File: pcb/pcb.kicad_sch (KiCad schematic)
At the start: 235 parts, among them J1 Conn_01x30

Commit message: Daughterboard
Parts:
- added H52, H53, H54, H55, H56, H57, H58: MountingHole, symbol Mechanical:MountingHole
- added MX059.2, MX079.2, MX099.2: MX-NoLED, MX_Only:MXOnly-1U-NoLED, symbol MX_Alps_Hybrid:MX-NoLED
- renumbered SCRL1 to CAP1, CAP1 to NUM1, NUM1 to SCRL1
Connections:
- net CAPS_LED: now also CAP1.2 (A), J1.29 (Pin_29); no longer J1.5 (Pin_5), NUM1.2 (A)
- net COL0: now also J1.28 (Pin_28); no longer J1.8 (Pin_8)
- net COL1: now also J1.27 (Pin_27); no longer J1.9 (Pin_9)
- net COL2: now also J1.26 (Pin_26); no longer J1.10 (Pin_10)
- net COL3: now also J1.23 (Pin_23); no longer J1.11 (Pin_11)
- net COL4: now also J1.22 (Pin_22); no longer J1.12 (Pin_12)
- net COL5: now also J1.11 (Pin_11); no longer J1.13 (Pin_13)
- net COL6: now also J1.10 (Pin_10); no longer J1.14 (Pin_14)
- net COL7: now also J1.7 (Pin_7); no longer J1.15 (Pin_15)
- net COL8: now also J1.5 (Pin_5); no longer J1.16 (Pin_16)
- net COL9: now also J1.4 (Pin_4), MX059.2.1 (COL), MX079.2.1 (COL), MX099.2.1 (COL); no longer J1.17 (Pin_17)
- net NUM_LED: now also J1.3 (Pin_3), NUM1.2 (A); no longer J1.7 (Pin_7), SCRL1.2 (A)
- net RE1: now also J1.9 (Pin_9); no longer J1.2 (Pin_2)
- net RE2: now also J1.8 (Pin_8); no longer J1.3 (Pin_3)
- net RE3: now also J1.6 (Pin_6); no longer J1.4 (Pin_4)
- net ROW0: now also J1.25 (Pin_25); no longer J1.18 (Pin_18)
- net ROW1: now also J1.21 (Pin_21); no longer J1.19 (Pin_19)
- net ROW10: now also J1.13 (Pin_13); no longer J1.28 (Pin_28)
- net ROW11: now also J1.12 (Pin_12); no longer J1.29 (Pin_29)
- net ROW3: now also J1.19 (Pin_19); no longer J1.21 (Pin_21)
- net ROW4: now also J1.18 (Pin_18); no longer J1.22 (Pin_22)
- net ROW5: now also J1.17 (Pin_17); no longer J1.23 (Pin_23)
- net ROW7: now also J1.16 (Pin_16); no longer J1.25 (Pin_25)
- net ROW8: now also J1.15 (Pin_15); no longer J1.26 (Pin_26)
- net ROW9: now also J1.14 (Pin_14); no longer J1.27 (Pin_27)
- net SCRL_LED: now also J1.2 (Pin_2), SCRL1.2 (A); no longer CAP1.2 (A), J1.6 (Pin_6)
- net at D36.1 (A), MX026.2 (ROW): no longer MX086.1.2 (ROW)
- net at D53.2 (A), MX099.2 (ROW): now also MX099.2.2 (ROW)
- net at D41.1 (A), MX086.2 (ROW): now also MX086.1.2 (ROW)
- net at D49.2 (A), MX059.2 (ROW): now also MX059.2.2 (ROW)
- net at D42.1 (A), MX096.2 (ROW): now also MX096.275.2 (ROW)
- net at D51.2 (A), MX079.2 (ROW): now also MX079.2.2 (ROW)
- net at D37.1 (A), MX036.2 (ROW), MX036.2.2 (ROW): no longer MX096.275.2 (ROW)
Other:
- moved on the sheet: MX086.1, MX096.275

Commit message: daughterboard rewire
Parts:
- renumbered MX052 to MX112, MX053 to MX113, MX053.7 to MX113.7, MX054 to MX114, MX055 to MX115
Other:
- moved on the sheet: D17, D28, MX112, MX113, MX113.7, MX114, MX115

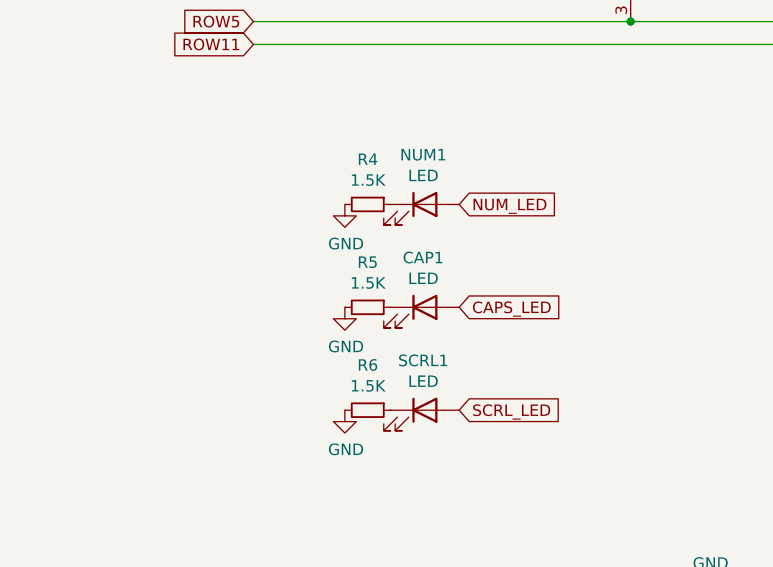
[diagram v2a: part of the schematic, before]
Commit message: Update PCB silkscreen
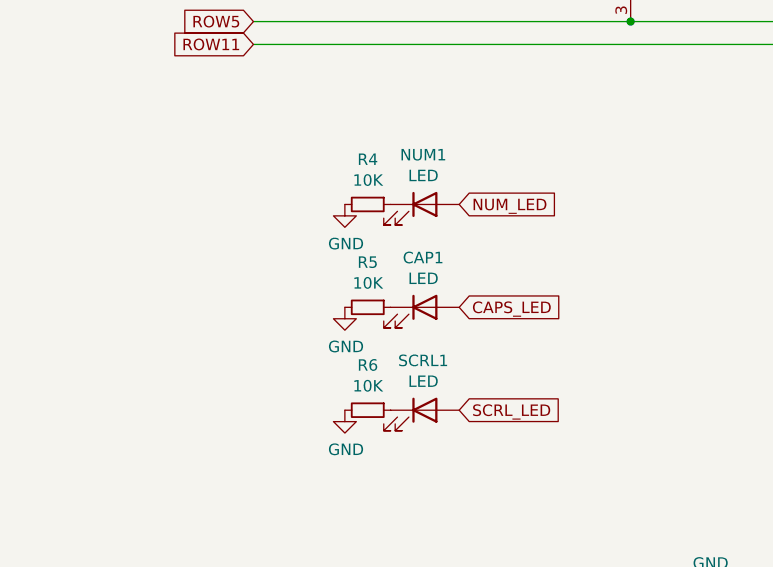
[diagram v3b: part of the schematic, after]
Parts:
- R4, R5, R6: value 1.5K -> 10K
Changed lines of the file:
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@@
     (in_bom yes) (on_board yes)
     (property "Reference" "R5" (id 0) (at 82.55 237.5916 90))
-    (property "Value" "1.5K" (id 1) (at 82.55 239.903 90))
+    (property "Value" "10K" (id 1) (at 82.55 239.903 90))
     (property "Footprint" "Resistor_THT:R_Axial_DIN0204_L3.6mm_D1.6mm_P5.08mm_Horizontal" (id 2) (at 82.55 242.57 0)
       (effects (font (size 1.27 1.27)) hide)
@@
     (in_bom yes) (on_board yes)
     (property "Reference" "R4" (id 0) (at 82.55 226.1616 90))
-    (property "Value" "1.5K" (id 1) (at 82.55 228.473 90))
+    (property "Value" "10K" (id 1) (at 82.55 228.473 90))
     (property "Footprint" "Resistor_THT:R_Axial_DIN0204_L3.6mm_D1.6mm_P5.08mm_Horizontal" (id 2) (at 82.55 231.14 0)
       (effects (font (size 1.27 1.27)) hide)
@@
     (in_bom yes) (on_board yes)
     (property "Reference" "R6" (id 0) (at 82.55 249.0216 90))
-    (property "Value" "1.5K" (id 1) (at 82.55 251.333 90))
+    (property "Value" "10K" (id 1) (at 82.55 251.333 90))
     (property "Footprint" "Resistor_THT:R_Axial_DIN0204_L3.6mm_D1.6mm_P5.08mm_Horizontal" (id 2) (at 82.55 254 0)
       (effects (font (size 1.27 1.27)) hide)
@@
     )
     (path "/594149a8-dcf4-477c-8bc6-ce49fe795a88"
-      (reference "R4") (unit 1) (value "1.5K") (footprint "Resistor_THT:R_Axial_DIN0204_L3.6mm_D1.6mm_P5.08mm_Horizontal")
+      (reference "R4") (unit 1) (value "10K") (footprint "Resistor_THT:R_Axial_DIN0204_L3.6mm_D1.6mm_P5.08mm_Horizontal")
     )
     (path "/3e587754-08bf-4e2f-861f-e6f342837f7f"
-      (reference "R5") (unit 1) (value "1.5K") (footprint "Resistor_THT:R_Axial_DIN0204_L3.6mm_D1.6mm_P5.08mm_Horizontal")
+      (reference "R5") (unit 1) (value "10K") (footprint "Resistor_THT:R_Axial_DIN0204_L3.6mm_D1.6mm_P5.08mm_Horizontal")
     )
     (path "/d9e43349-c262-4673-9be5-82fe3b06b371"
-      (reference "R6") (unit 1) (value "1.5K") (footprint "Resistor_THT:R_Axial_DIN0204_L3.6mm_D1.6mm_P5.08mm_Horizontal")
+      (reference "R6") (unit 1) (value "10K") (footprint "Resistor_THT:R_Axial_DIN0204_L3.6mm_D1.6mm_P5.08mm_Horizontal")
     )
     (path "/956d7a0d-344f-4ad9-8679-52e88c72815a"
